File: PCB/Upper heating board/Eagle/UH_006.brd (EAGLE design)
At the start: 142.8 x 97.5 mm, 5 parts, among them X3 MKDSN1,5/4-5,08

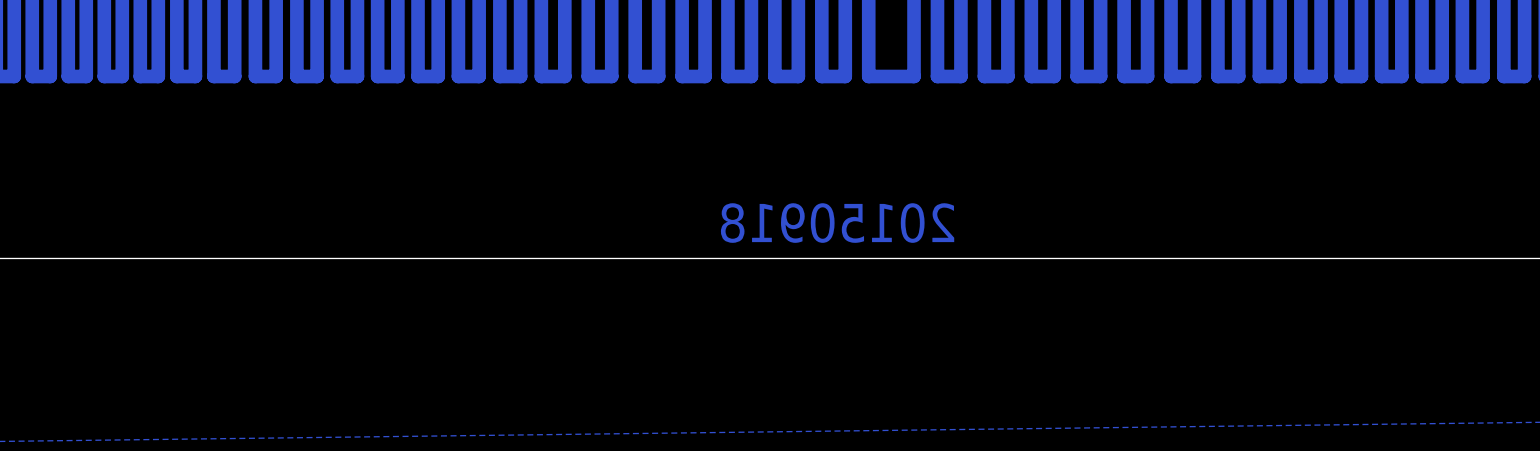
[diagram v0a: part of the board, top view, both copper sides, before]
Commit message: PCB modification, CERN license
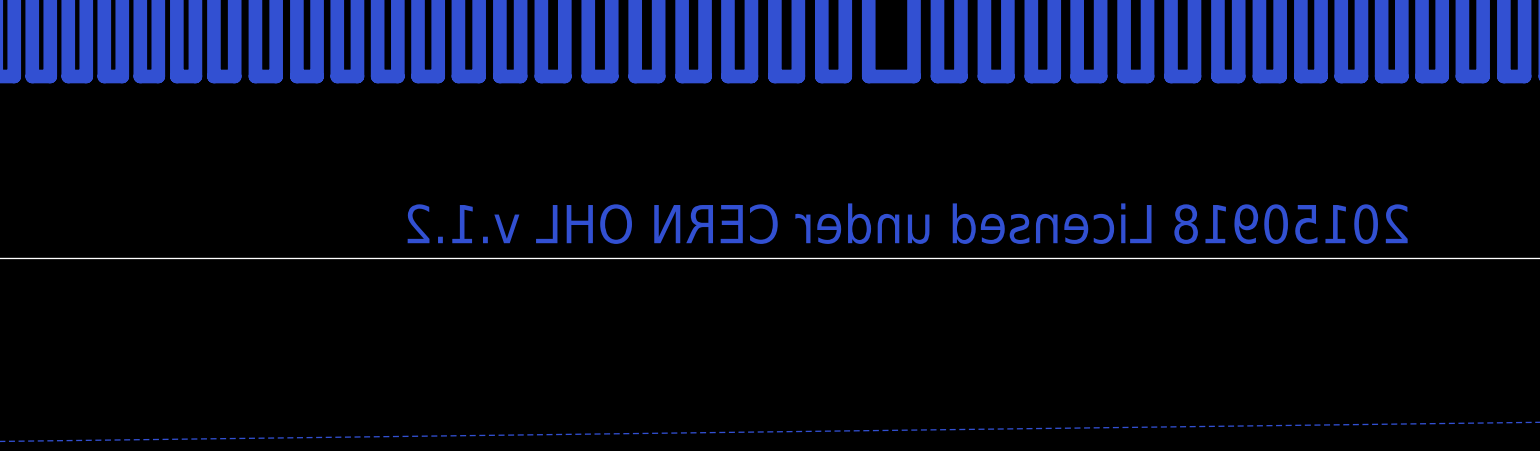
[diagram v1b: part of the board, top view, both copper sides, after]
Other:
- board text added: "20150918 Licensed under CERN OHL v.1.2"
- board text removed: "20150918"
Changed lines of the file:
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@@
 <plain>
 <text x="54.7086" y="96.1384" size="1.778" layer="16" font="vector" ratio="15" rot="MR180">Miriam</text>
-<text x="71.501" y="0.762" size="1.778" layer="16" font="vector" ratio="15" rot="MR0">20150918</text>
+<text x="92.6084" y="0.7112" size="1.778" layer="16" font="vector" ratio="15" rot="MR0">20150918 Licensed under CERN OHL v.1.2</text>
 <text x="131.794" y="55.508" size="1.27" layer="21" font="vector" rot="R270">+12V</text>
 <text x="131.794" y="44.459" size="1.27" layer="21" rot="R270">TH1</text>
@@
 <text x="131.794" y="40.236" size="1.27" layer="21" font="vector" rot="R270">UP_HEAT</text>
 <rectangle x1="40.6182" y1="93.827" x2="76.61" y2="96.748" layer="42"/>
-<rectangle x1="56.896" y1="0.508" x2="71.755" y2="2.794" layer="42"/>
 <wire x1="0" y1="5" x2="5" y2="0" width="0.02" layer="20" curve="90"/>
 <wire x1="5" y1="0" x2="137.76" y2="0" width="0.02" layer="20"/>
@@
 <text x="1.6764" y="36.3248" size="1.778" layer="26" font="vector" ratio="15" rot="MR90">Upper heater 006</text>
 <text x="54.8102" y="96.24" size="1.778" layer="26" font="vector" ratio="15" rot="MR180">Miriam</text>
-<text x="71.2724" y="0.5842" size="1.778" layer="26" font="vector" ratio="15" rot="MR0">20150918</text>
+<text x="92.6592" y="0.762" size="1.778" layer="26" font="vector" ratio="15" rot="MR0">20150918 Licensed under CERN OHL v.1.2</text>
+<rectangle x1="32.3088" y1="0.3556" x2="93.98" y2="3.0988" layer="42"/>
 </plain>
 <attributes>
